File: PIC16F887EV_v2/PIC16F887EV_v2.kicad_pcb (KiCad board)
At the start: 2 copper layers, 100 x 100 mm, 101 parts, among them J1 USB_C_Receptacle_USB2.0_14P, Q1 2N3904, Q2 2N3904, Q3 2N3904, Q5 2N3904, SW1 SW_Push, SW10 SW_Push, SW11 SW_Push, SW12 SW_Push, SW13 SW_Push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

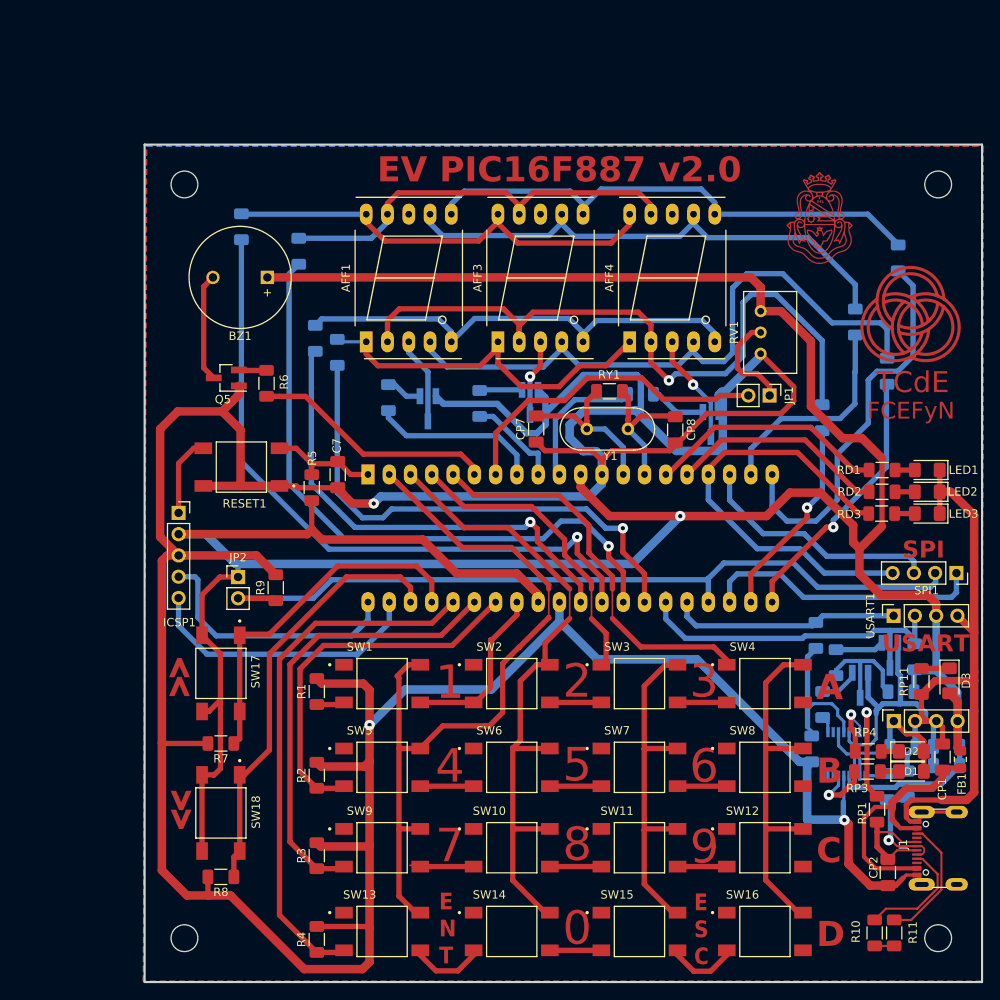
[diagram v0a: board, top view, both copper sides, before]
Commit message: Correccion errores v1, y finalizacion V2
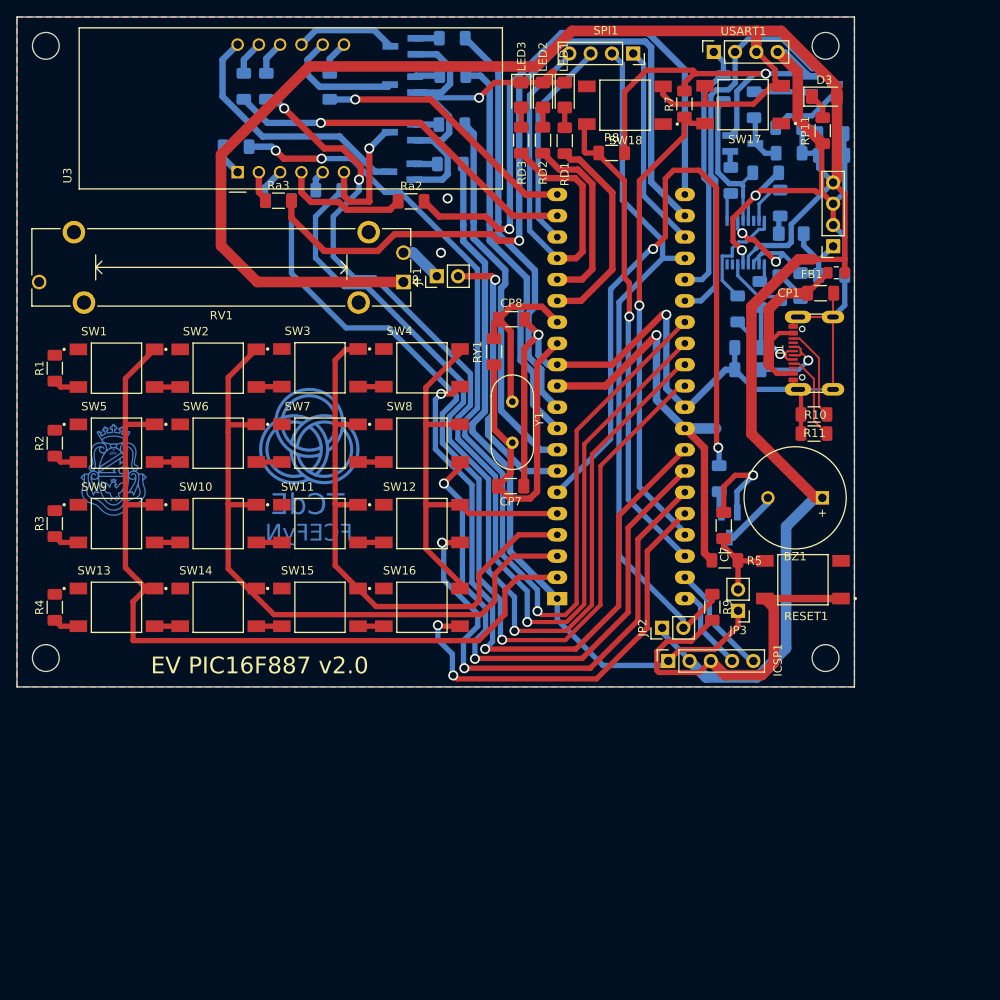
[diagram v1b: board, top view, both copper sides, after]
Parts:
- removed AFF1, AFF3, AFF4: LTS-6980HR, Display_7Segment:7SegmentLED_LTS6760_LTS6780
- removed REF1, REF2: MountingHole_3.2mm_M3, MountingHole:MountingHole_3.2mm_M3
- removed the REF4 at (110.0, 110.0)
- added JP3: Jumper_2_Bridged, Connector_PinHeader_2.54mm:PinHeader_1x02_P2.54mm_Vertical, F.Cu at (86.1, 70.9)
- added Q4: 2N3904, Huellas:SOT-23_Handsoldering-mod, B.Cu at (46.0, 13.8)
- added RD6: 4.7k, Resistor_SMD:R_1206_3216Metric_Pad1.30x1.75mm_HandSolder, B.Cu at (51.9, 12.9)
- added REF4: MountingHole_3.2mm_M3, MountingHole:MountingHole_3.2mm_M3, F.Cu at (96.5, 3.45)
- added REF4: MountingHole_3.2mm_M3, MountingHole:MountingHole_3.2mm_M3, F.Cu at (96.5, 76.5)
- added REF4: MountingHole_3.2mm_M3, MountingHole:MountingHole_3.2mm_M3, F.Cu at (3.45, 3.45)
- added U3: CC56-12EWA, Display_7Segment:CA56-12EWA, F.Cu at (26.4, 18.5)
- CP2, D1, D2, G*** (x2), Q5, R6, RP1, RP3, RP4: moved to B.Cu
- RV1: value R_Potentiometer -> R_Potentiometer_MountingPin; footprint Potentiometer_THT:Potentiometer_Bourns_3299W_Vertical -> Potentiometer_THT:Potentiometer_Bourns_PTA3043_Single_Slide
- Ra2, Ra3: moved to F.Cu
- TCdE FCEFYN: moved to B.Cu (x2)
- moved R8 98.2 mm to (71.0, 16.2), turned to 0 degrees
- moved SW18 97.3 mm to (72.6, 10.5), turned to 180 degrees
- moved R7 94.3 mm to (79.7, 10.4), turned to 90 degrees
- moved SW17 92.2 mm to (86.7, 10.5), turned to 180 degrees
- moved G*** 89.5 mm to (11.5, 54.1), turned to 180 degrees (x2)
- moved Ra8 78.2 mm to (27.1, 8.28)
- moved CP5 76.7 mm to (97.2, 13.9), turned to 180 degrees
- moved TCdE FCEFYN 73.3 mm to (34.9, 50.6), turned to 180 degrees (x2)
- moved SPI1 73.1 mm to (73.6, 4.36)
- moved CP6 71.9 mm to (97.3, 16.5), turned to 180 degrees
- moved D3 71.3 mm to (96.4, 9.52), turned to 0 degrees
- moved BZ1 71.3 mm to (96.2, 57.4)
- moved Ra1 70.9 mm to (37.3, 8.28)
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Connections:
- C7 pad 1: MCLR -> Net-(JP3-B)
- Q1 pad 3: Net-(Q1-C) -> DISPLAY1
- Q2 pad 3: Net-(Q2-C) -> DISPLAY2
- Q3 pad 3: Net-(Q3-C) -> DISPLAY3
- R5 pad 2: MCLR -> Net-(JP3-B)
- RD12 pad 2: RE0 -> MCLR
- RD4 pad 2: RE1 -> RE2
- RD5 pad 2: RE2 -> RE1
- RESET1 pad 2: MCLR -> Net-(JP3-B)
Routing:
- net GND: track 593.7 -> 328.7 mm, vias 3 -> 9
- net d: track 84.4 -> 3.72 mm, vias 1 -> 0
- net RD3: track 24.0 -> 90.5 mm
- net MCLR: track 23.0 -> 87.9 mm
- net c: track 78.3 -> 15.2 mm
- net RD4: track 61.8 -> 122.8 mm, vias 1 -> 3
- net a: track 63.6 -> 4.18 mm
- net b: track 62.4 -> 4.13 mm
- net RD7: track 56.7 -> 111.3 mm
- net RA4: track 29.2 -> 83.7 mm, vias 0 -> 2
- net DP: track 56.0 -> 4.17 mm
- net g: track 54.3 -> 2.49 mm
- net RD5: track 77.1 -> 126.4 mm, vias 1 -> 3
- net RB0: track 40.1 -> 88.9 mm, vias 0 -> 2
- net f: track 50.6 -> 4.11 mm
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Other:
- board size 100 x 100 mm -> 100 x 80 mm
- board text removed: "0"
- board text removed: "1"
- board text removed: "2"
- board text removed: "3"
- board text removed: "4"
- board text removed: "5"
- board text removed: "6"
- board text removed: "7"
- board text removed: "8"
- board text removed: "9"
- board text removed: "A"
- board text removed: "B"
- board text removed: "C"
- board text removed: "D"
- board text removed: "E N T"
- board text removed: "E S C"
- board text removed: "SPI"
- board text removed: "USART"
- board text removed: "»"

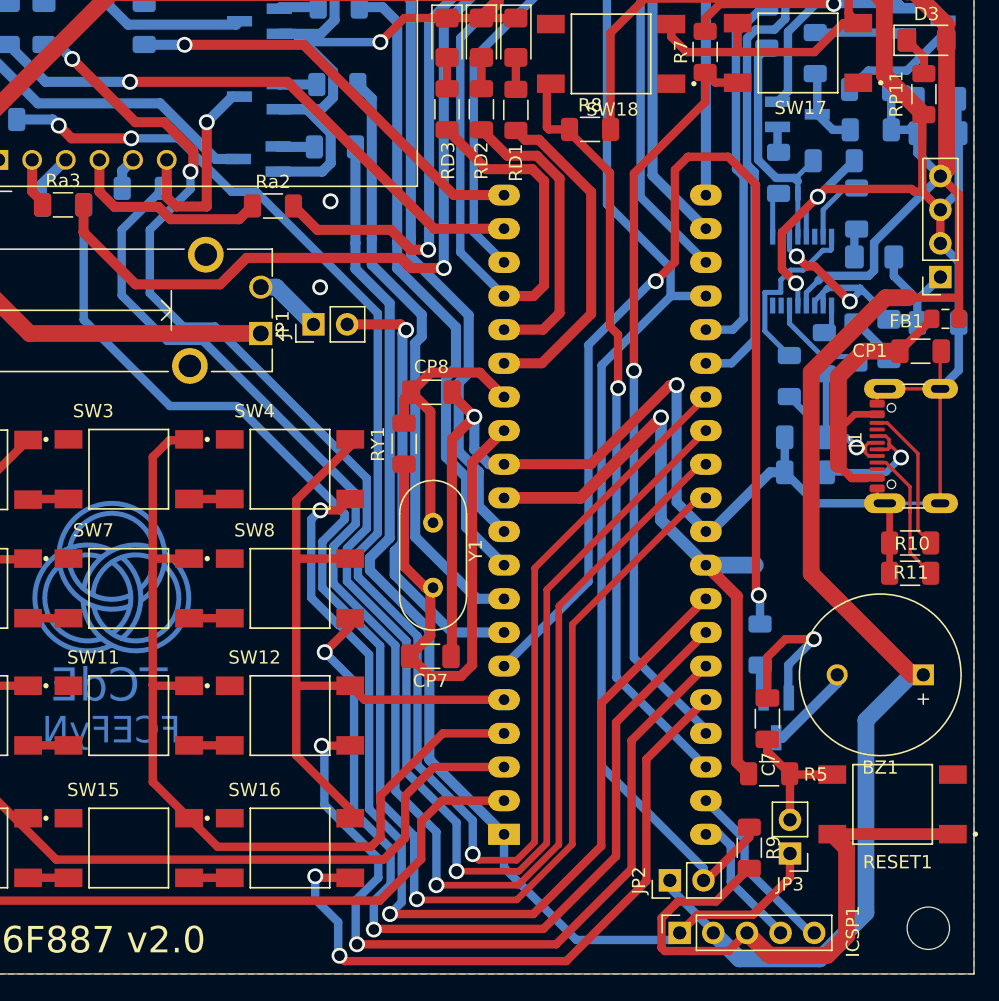
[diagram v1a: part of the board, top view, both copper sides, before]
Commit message: Ordenamiento y equidistanciamiento en RD y  RB
Cambie el ancho de pistas, las equidistancie entre  si, de modo que que no queden algunas muy pegadas
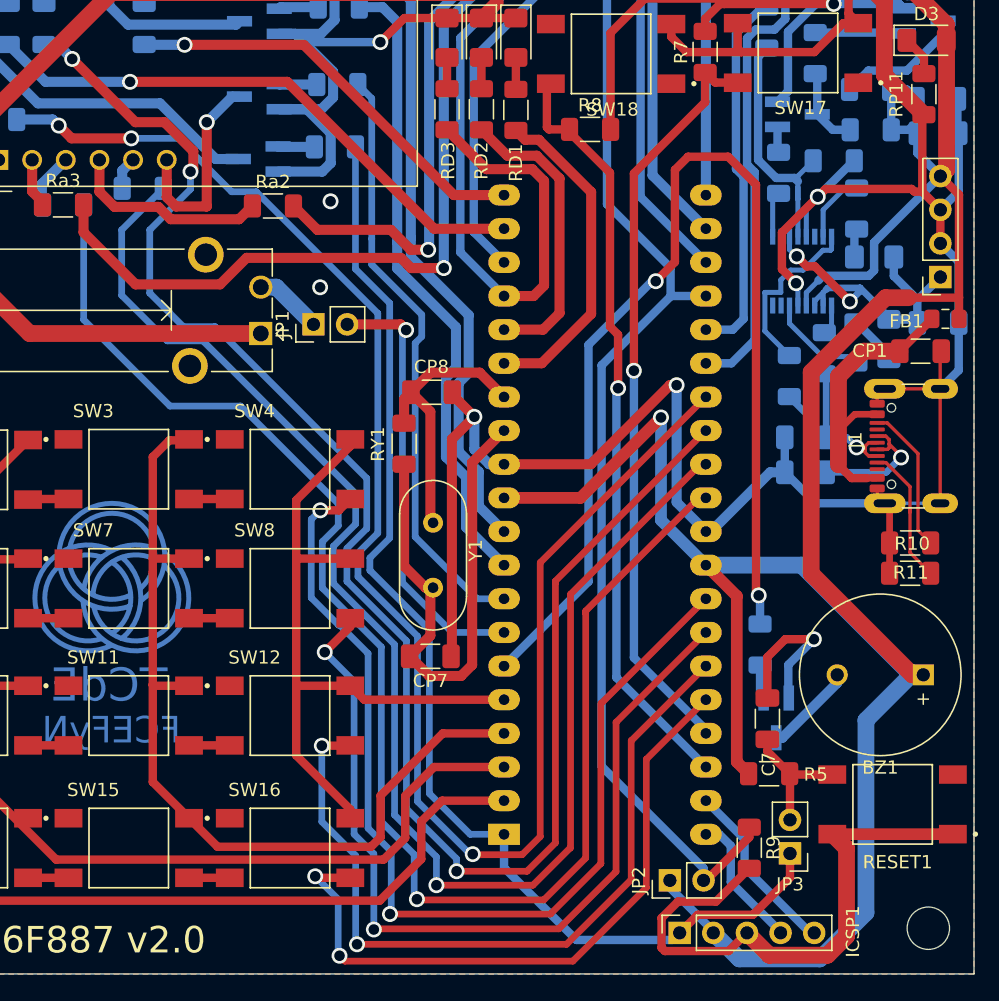
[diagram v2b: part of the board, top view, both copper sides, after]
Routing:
- net +5V: track 324.8 -> 340.1 mm
- net MCLR: track 87.9 -> 89.4 mm
- net RD7: track 111.3 -> 112.3 mm
- net RB2: track 72.7 -> 72.0 mm
- net RD6: track 110.8 -> 111.4 mm
